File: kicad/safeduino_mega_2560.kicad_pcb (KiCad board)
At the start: 4 copper layers, 134.5 x 63.9 mm, 109 parts, among them X1 USBB-1J

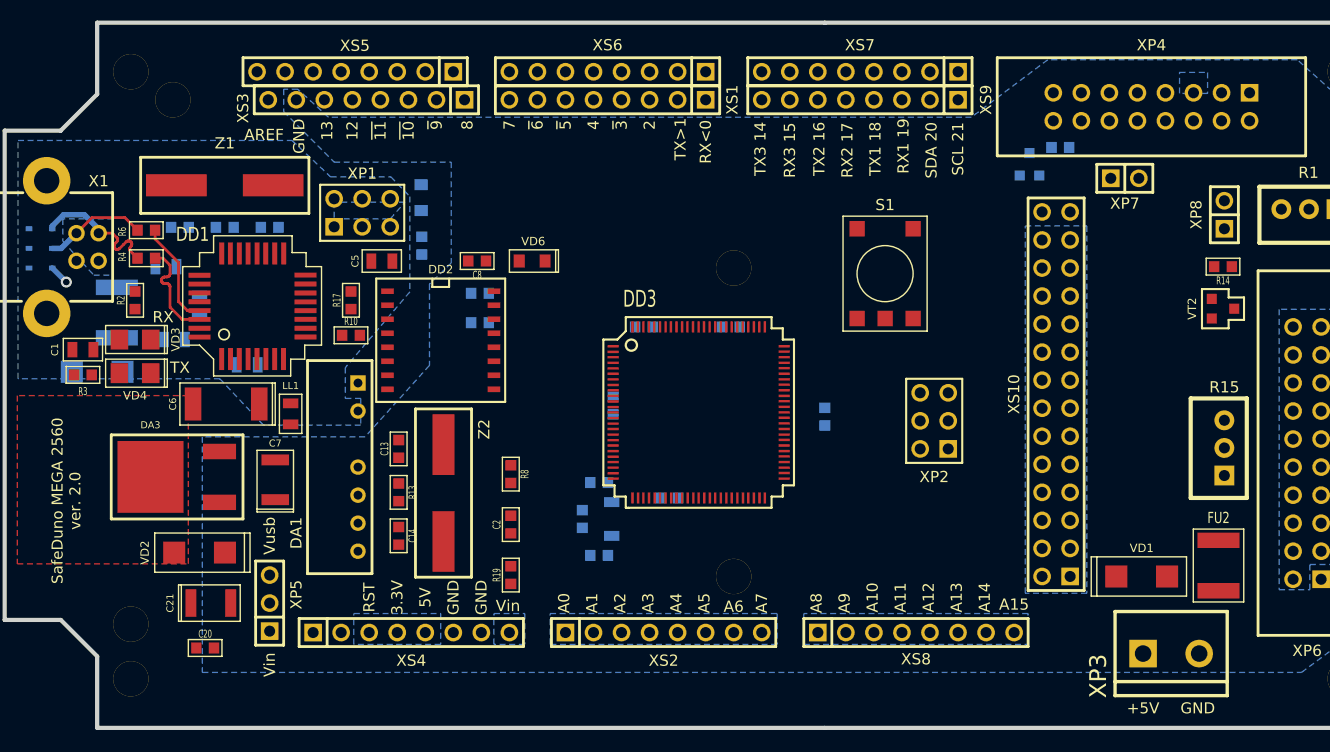
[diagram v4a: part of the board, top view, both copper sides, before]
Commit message: Продолжил переделывать печатную плату SafeDuino MEGA 2560.
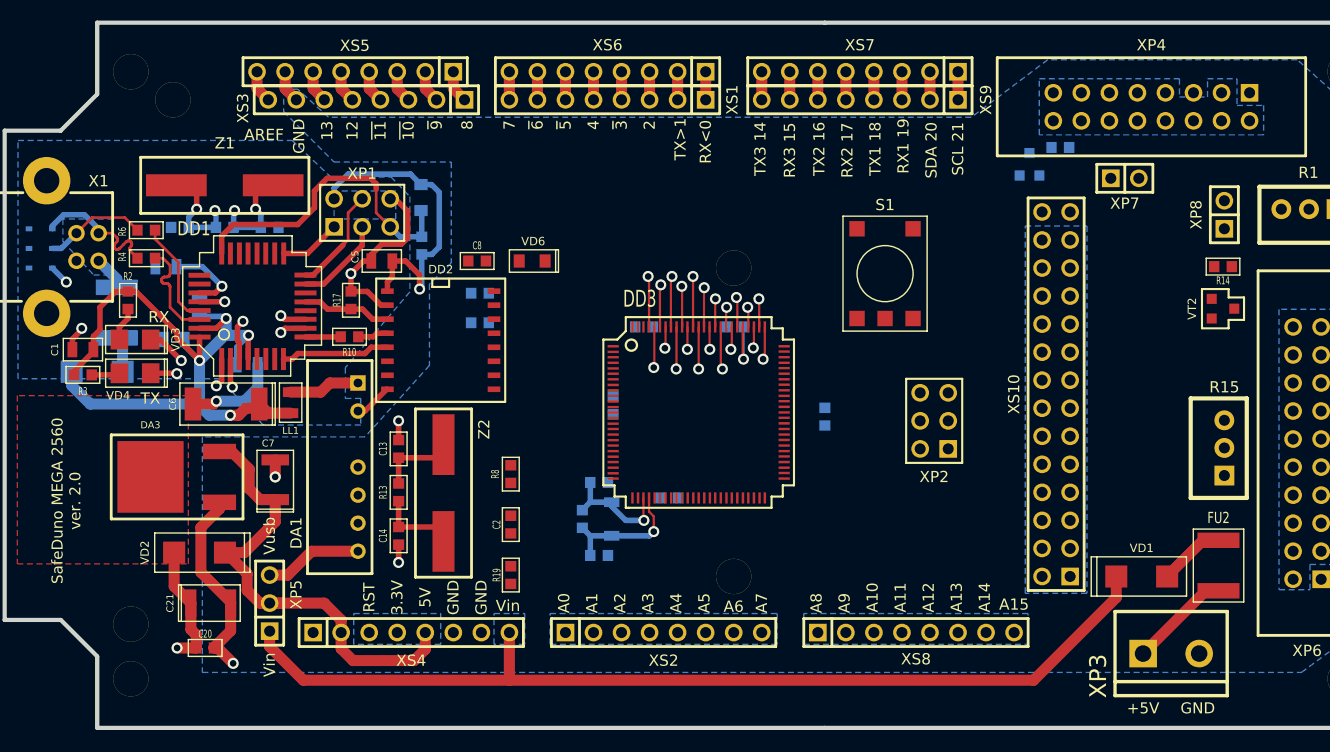
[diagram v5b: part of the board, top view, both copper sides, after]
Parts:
- moved LL1 1.02 mm to (78.0, 124.0)
- moved R2 0.64 mm to (63.2, 114.7)
- moved C18 0.38 mm to (118.2, 117.1)
- moved R10 0.18 mm to (83.3, 118.0)
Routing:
- net /5V_USB: track 0.00 -> 119.7 mm, vias 0 -> 5
- net /VCCIN: track 0.00 -> 88.7 mm
- net /MPU_VCC: track 0.00 -> 49.3 mm, vias 0 -> 1
- net /GND_USB: track 0.00 -> 37.0 mm, vias 0 -> 5
- net /VCC3V3: track 0.00 -> 35.1 mm, vias 0 -> 1
- net /RESET_16U2: track 0.00 -> 28.9 mm
- net /GND: track 0.00 -> 28.5 mm, vias 0 -> 5
- net Net-(C4-Pad1): track 0.00 -> 28.4 mm, vias 0 -> 3
- net Net-(C3-Pad1): track 0.00 -> 28.2 mm, vias 0 -> 3
- net /TXI: track 0.00 -> 18.4 mm, vias 0 -> 2
- net /RXI: track 0.00 -> 17.2 mm, vias 0 -> 2
- net /PG4: track 0.00 -> 11.9 mm, vias 0 -> 1
- net /PG3: track 0.00 -> 10.6 mm, vias 0 -> 1
- net /PE1: track 0.00 -> 9.86 mm
- net /MOSI2: track 0.00 -> 9.70 mm
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
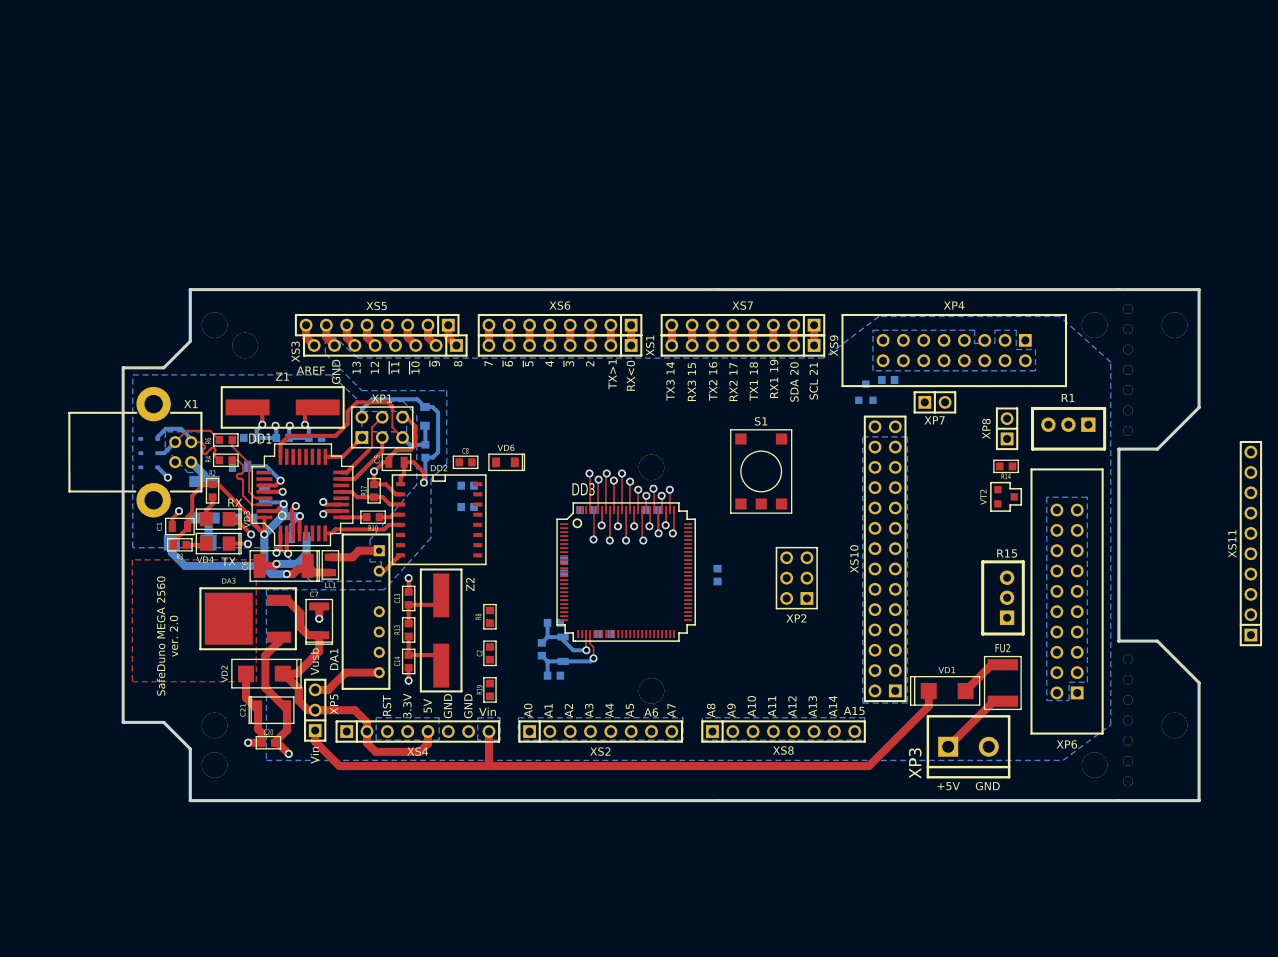
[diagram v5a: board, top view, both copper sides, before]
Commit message: Продолжил трассировку печатной платы SafeDuino MEGA 2560.
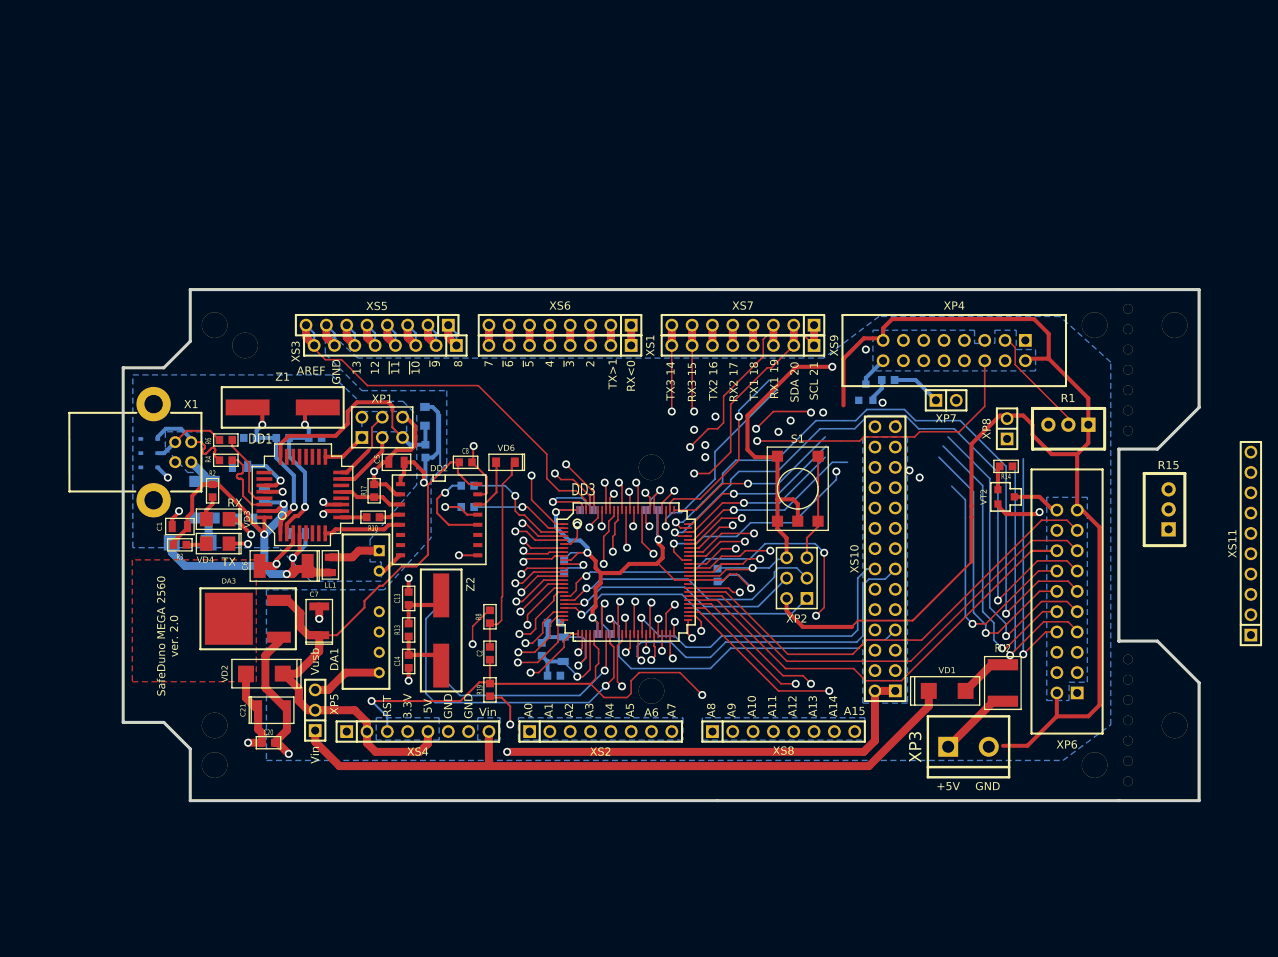
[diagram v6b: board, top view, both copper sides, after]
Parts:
- moved R15 23.0 mm to (182.8, 119.5)
- moved S1 5.06 mm to (136.4, 114.2)
- moved XP7 1.42 mm to (154.9, 103.4)
- moved C9 0.52 mm to (73.9, 120.0), turned to 0 degrees
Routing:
- net /MPU_VCC: track 49.3 -> 413.1 mm, vias 1 -> 6
- net /GND: track 28.5 -> 147.4 mm, vias 5 -> 15
- net /PE2: track 0.00 -> 93.0 mm, vias 0 -> 1
- net /PE6: track 0.00 -> 89.3 mm, vias 0 -> 1
- net /PE7: track 0.00 -> 85.5 mm, vias 0 -> 1
- net /PA4: track 0.00 -> 82.2 mm, vias 0 -> 2
- net /PA6: track 0.00 -> 80.1 mm, vias 0 -> 2
- net /RESET: track 0.00 -> 73.8 mm, vias 0 -> 2
- net /PH2: track 0.00 -> 67.1 mm, vias 0 -> 3
- net /PL1: track 0.00 -> 65.6 mm, vias 0 -> 1
- net /PB7: track 2.96 -> 67.2 mm, vias 0 -> 1
- net /PC3: track 0.00 -> 60.7 mm
- net /PB6: track 2.96 -> 63.3 mm, vias 0 -> 1
- net /PJ4: track 0.00 -> 60.1 mm, vias 0 -> 2
- net /PC5: track 0.00 -> 59.3 mm
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
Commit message: Закончил предварительную трассировку платы SafeDuino MEGA 2560.
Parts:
- FU2: moved to B.Cu
- XS11: value PBS-10 -> PBS-8; footprint IWconnectors:PIN_ARRAY_10x1 -> IWconnectors:PIN_ARRAY_8x1
- moved XS11 37.3 mm to (156.2, 115.6)
- moved R15 28.7 mm to (162.6, 140.0)
- moved FU2 6.90 mm to (155.3, 140.3)
- moved XP7 6.06 mm to (160.0, 106.7)
- moved XP2 3.73 mm to (136.1, 122.0), turned to 0 degrees
- moved XP8 3.42 mm to (160.0, 109.2), turned to 0 degrees
- moved VD1 2.13 mm to (154.4, 137.7), turned to 270 degrees
- moved C17 1.91 mm to (124.5, 125.2)
- moved R14 1.66 mm to (160.8, 111.8), turned to 0 degrees
- moved S1 1.28 mm to (136.3, 112.9)
- moved VT2 0.46 mm to (162.7, 115.1)
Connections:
- XS11 pad 1: /SS -> /PH7
- XS11 pad 2: /PE2 -> /PD4
- XS11 pad 3: /PE6 -> /PD5
- XS11 pad 4: /PE7 -> /PD6
- XS11 pad 5: /PD4 -> /PH2
- XS11 pad 6: /PD5 -> /PE7
- XS11 pad 7: /PD6 -> /PE6
- XS11 pad 8: /PH2 -> /PE2
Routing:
- net /PD4: track 2.48 -> 59.7 mm
- net /PD6: track 3.18 -> 55.7 mm
- net /PD5: track 4.39 -> 56.4 mm
- net /GND: track 147.4 -> 109.3 mm, vias 15 -> 14
- net /PC7: track 0.00 -> 37.5 mm
- net /PC6: track 6.70 -> 39.8 mm, vias 1 -> 0
- net /MPU_VCC: track 413.1 -> 384.7 mm, vias 6 -> 7
- net /RESET: track 73.8 -> 101.3 mm, vias 2 -> 1
- net /PH2: track 67.1 -> 93.9 mm
- net /PA0: track 60.5 -> 85.0 mm, vias 2 -> 3
- net /PA1: track 53.1 -> 76.2 mm
- net /PH7: track 55.2 -> 75.0 mm
- net /PJ4: track 60.1 -> 42.4 mm, vias 2 -> 1
- net /PA6: track 80.1 -> 64.4 mm, vias 2 -> 4
- net /PE2: track 93.0 -> 77.9 mm
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
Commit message: Оптимизировал трассировку печатной платы.
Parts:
- moved VD6 9.28 mm to (99.1, 120.4), turned to 270 degrees
- moved C14 7.87 mm to (87.8, 128.1), turned to 90 degrees
- moved C13 7.84 mm to (87.8, 136.0), turned to 270 degrees
- moved R1 1.52 mm to (172.7, 104.9)
- moved R8 1.14 mm to (97.9, 131.6)
- moved R19 1.14 mm to (97.9, 138.4)
- turned R13 to 90 degrees
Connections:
- Z2 pad 1: Net-(C13-Pad1) -> Net-(C14-Pad1)
- Z2 pad 2: Net-(C14-Pad1) -> Net-(C13-Pad1)
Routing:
- net /PG5: track 42.9 -> 28.5 mm
- net /PH2: track 93.9 -> 80.3 mm
- net Net-(C14-Pad1): track 54.3 -> 41.3 mm, vias 2 -> 0
- net Net-(C2-Pad2): track 24.6 -> 12.3 mm
- net Net-(C13-Pad1): track 53.1 -> 42.5 mm, vias 2 -> 0
- net /PH3: track 53.3 -> 43.0 mm
- net /PH4: track 54.8 -> 44.8 mm
- net /PE3: track 43.2 -> 34.3 mm
- net /PE2: track 77.9 -> 69.9 mm
- net /5V_USB: track 137.4 -> 129.6 mm
- net /GND: track 109.3 -> 101.9 mm
- net /PL6: track 47.0 -> 41.3 mm, vias 1 -> 2
- net /PB5: track 60.6 -> 55.0 mm
- net /ADC0: track 45.1 -> 39.5 mm
- net /PB7: track 67.2 -> 61.9 mm
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- added copper zone on B.Cu, net /VCC3V3
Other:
- board text added: "IOREF"
